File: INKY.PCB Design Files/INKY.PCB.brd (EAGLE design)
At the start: 55.8 x 40.9 mm, 34 parts, among them J1-PROG RJ45-8, J2 RJ45-8, U1 MC9S08SH8CTG, U3 RS485SOIC

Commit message: Still routing
~ 95% done
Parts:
- moved U3 2.00 mm to (-3.75, -6.22)
- moved U$14 1.31 mm to (8.45, 0.40)
- moved U$23 1.30 mm to (17.4, -9.20)
- moved U$21 1.21 mm to (16.6, -13.8)
- moved U$13 1.12 mm to (-0.90, -9.50)
- moved U$22 1.05 mm to (17.4, -11.6)
- moved U$20 0.65 mm to (0.00, -15.9)
- moved C1 0.47 mm to (-2.56, 11.7)
- moved U$2 0.40 mm to (-16.0, -17.6), flipped to the bottom
- moved U$8 0.40 mm to (-16.0, -17.6), flipped to the top
- moved U$5 0.35 mm to (10.4, -13.6)
- moved C2 0.34 mm to (2.04, 11.6)
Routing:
- net GND: track 123.3 -> 200.9 mm
- net +3V3: track 41.7 -> 105.7 mm
- net ACK: track 22.4 -> 70.4 mm, vias 0 -> 1
- net N$6: track 0.00 -> 39.7 mm, vias 0 -> 1
- net +5V: track 189.1 -> 221.6 mm, vias 2 -> 4
- net N$5: track 0.00 -> 30.3 mm, vias 0 -> 1
- net RST: track 3.00 -> 16.9 mm, vias 0 -> 1
- net RX: track 28.7 -> 14.8 mm
- net BDM: track 10.8 -> 5.22 mm, vias 0 -> 1
- net 485N: track 59.1 -> 61.5 mm
- net N$29: track 28.0 -> 30.2 mm
- net N$30: track 23.5 -> 25.4 mm
- net N$31: track 15.0 -> 16.7 mm
- net DIR: track 12.6 -> 11.0 mm
- net N$7: track 9.75 -> 8.25 mm
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
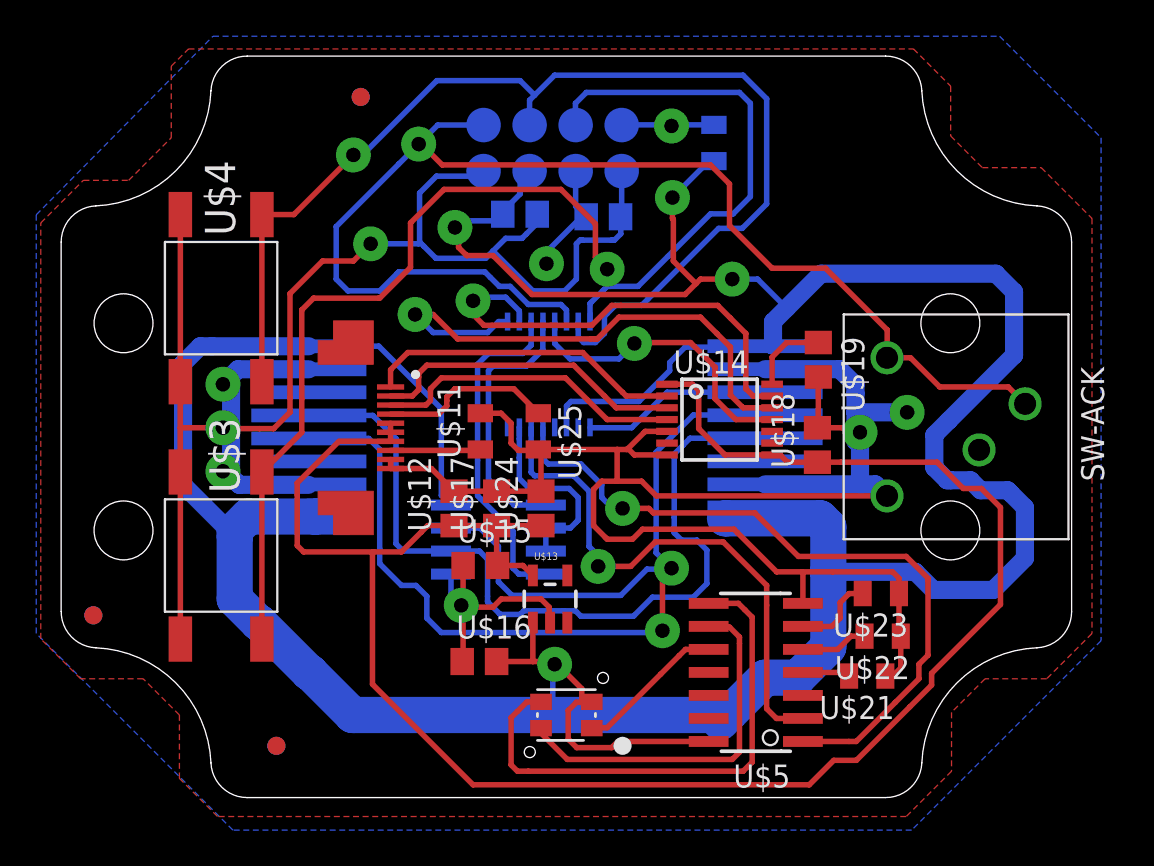
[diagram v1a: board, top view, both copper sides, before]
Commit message: Inky finishing
Done routing, need to fix angles.
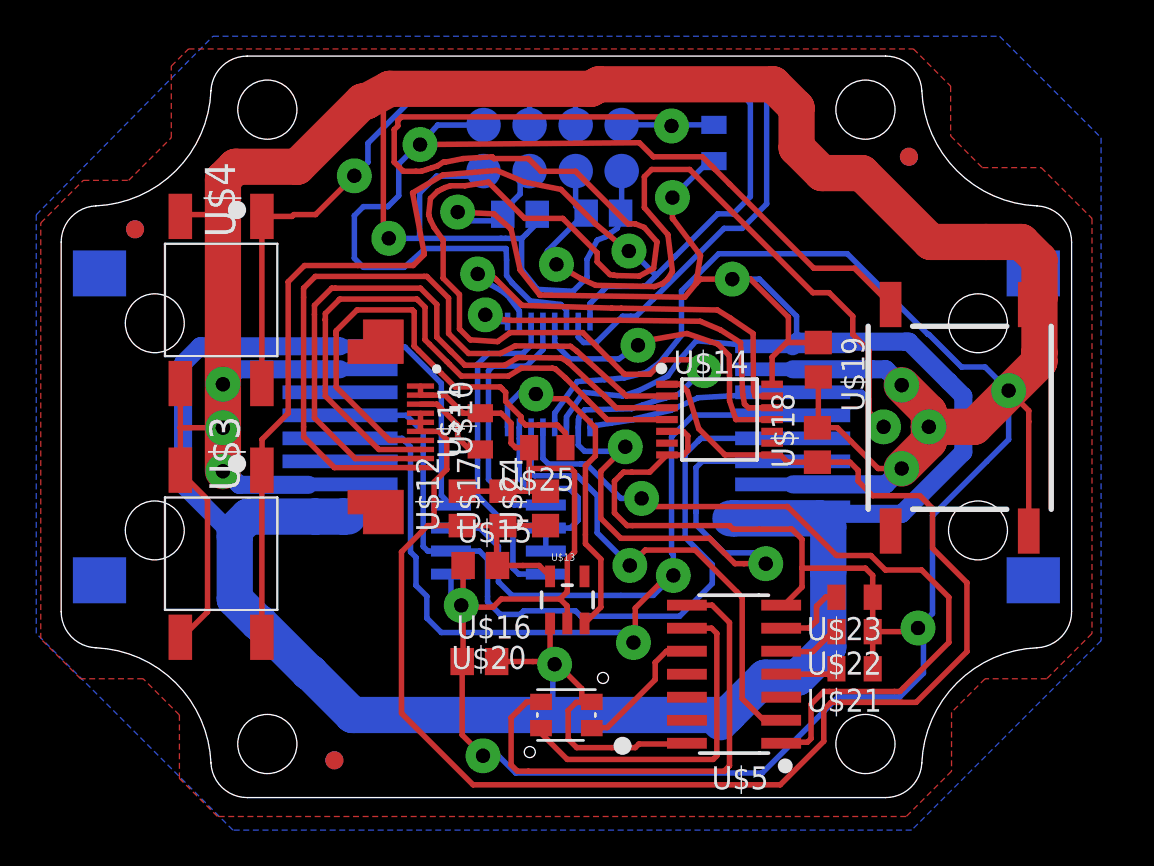
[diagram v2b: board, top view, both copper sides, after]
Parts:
- J1-PROG, J2: value RJ45-8 -> RJ45-8MOLEX_0955406886; device GW-devices:MOLEX-0955016649 -> GW-devices:RJ45_GUIDE
- SW-ACK: value SWITCH-TACTILE-320.01E11WHT -> SWITCH-TACTILE-5E/5GSH9; device GW-devices:SWITCH-TACTILE-320.01E11WHT -> GW-devices:SWITCH_TACTILE-5E/5GSH9
- U$10: value 52745-1097 -> (none); device KW2:52745-1097 -> KW2:FPC
- U$20: device KW2:RGBLED -> KW2:PLCC4_SMALL
- moved U$6 30.4 mm to (18.9, 14.9), flipped to the bottom
- moved U$9 30.4 mm to (18.9, 14.9), flipped to the top
- moved U$1 21.4 mm to (-23.8, 10.9)
- moved U$7 21.4 mm to (-23.8, 10.9)
- moved J2 11.9 mm to (-12.5, 0.00)
- moved J1-PROG 8.70 mm to (12.5, 0.00)
- moved U$2 3.30 mm to (-12.8, -18.4)
- moved U$8 3.30 mm to (-12.8, -18.4)
- moved U$10 1.65 mm to (-9.00, 0.00)
- moved U$22 1.57 mm to (15.9, -11.3)
- moved U$23 1.46 mm to (15.9, -9.40)
- moved U$5 1.20 mm to (9.25, -13.7)
- moved U$25 1.03 mm to (-1.05, -1.15), turned to 180 degrees
- moved U$13 0.95 mm to (0.05, -9.55)
- moved U$21 0.81 mm to (15.9, -13.3)
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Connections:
- removed net +3V3: U$10.P$5, U$10.P$6, U$10.P$7, U$12.1, U$13.5, U$14.1, U$14.8, U$15.2, U$17.1, U$18.1, U$24.1
- new net GMD: U$10.P$4, U$10.P$5, U$10.P$6, U$12.1, U$13.5, U$14.1, U$14.8, U$15.2, U$17.1, U$18.1, U$24.1
- net ACK: no longer SW-ACK.P$2
- net GND: now also U$10.P$1, U$10.P$2; no longer U$10.P$10, U$10.P$9
- net N$2: now also U$10.P$10; no longer U$10.P$1
- net N$3: now also U$10.P$9; no longer U$10.P$2
- net N$32: now also U$10.P$3; no longer U$10.P$8
- net N$33: now also U$10.P$7; no longer U$10.P$4
- net N$4: now also U$10.P$8; no longer U$10.P$3
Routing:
- net GND: track 200.9 -> 359.7 mm, vias 7 -> 11
- net BDM: track 5.22 -> 119.8 mm, vias 1 -> 4
- net +3V3: track 105.7 -> 0.00 mm
- net GMD: track 0.00 -> 94.8 mm
- net RST: track 16.9 -> 59.2 mm, vias 1 -> 2
- net N$2: track 17.6 -> 39.7 mm
- net N$3: track 17.5 -> 36.8 mm
- net N$1: track 0.00 -> 19.0 mm, vias 0 -> 1
- net N$33: track 9.58 -> 27.3 mm
- net N$4: track 17.2 -> 34.3 mm
- net ACK: track 70.4 -> 57.7 mm
- net +5V: track 221.6 -> 209.8 mm
- net N$29: track 30.2 -> 21.9 mm
- net INC_DOWN: track 72.9 -> 76.9 mm
- net N$5: track 30.3 -> 27.1 mm
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
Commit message: Inky v0.1
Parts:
- moved U1 0.20 mm to (-0.77, 2.89)
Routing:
- net GND: track 359.7 -> 358.6 mm
- net +5V: track 209.8 -> 208.9 mm
- net N$6: track 42.5 -> 41.7 mm
- net BDM: track 119.8 -> 120.5 mm
- net N$5: track 27.1 -> 26.4 mm
- net DIR: track 11.0 -> 10.4 mm
- net N$29: track 21.9 -> 21.3 mm

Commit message: Inky 0.2
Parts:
- U$11, U$25: value (none) -> 10K
- moved U$20 32.6 mm to (0.00, 16.7)
- moved U$5 31.2 mm to (-10.2, 10.7)
- moved U$21 28.2 mm to (-2.70, 7.85)
- moved U$22 28.1 mm to (-2.70, 9.70)
- moved U$23 28.0 mm to (-2.70, 11.5)
- moved U$16 17.3 mm to (12.4, -11.2), turned to 90 degrees
- moved U$15 17.2 mm to (12.4, -6.40), turned to 270 degrees
- moved U$12 15.5 mm to (7.85, -11.9), turned to 270 degrees
- moved U$17 15.4 mm to (10.0, -11.9), turned to 270 degrees
- moved U$13 15.1 mm to (15.1, -8.50)
- moved U$10 13.9 mm to (0.00, -10.6), turned to 0 degrees
- moved C2 13.1 mm to (15.1, 12.5), turned to 90 degrees
- moved U$24 11.5 mm to (9.85, -7.70)
- moved C1 7.38 mm to (-9.26, 8.63)
- moved U$11 6.55 mm to (-2.00, -6.20)
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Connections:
- net INC_DOWN: no longer U$3.2
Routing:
- net GND: track 358.6 -> 283.5 mm, vias 11 -> 12
- net BDM: track 120.5 -> 57.8 mm, vias 4 -> 3
- net GMD: track 94.8 -> 42.5 mm
- net +5V: track 208.9 -> 259.3 mm, vias 4 -> 5
- net N$1: track 18.9 -> 54.2 mm, vias 1 -> 3
- net ACK: track 57.9 -> 25.7 mm
- net N$6: track 41.7 -> 12.7 mm
- net N$33: track 27.3 -> 2.68 mm
- net N$2: track 39.9 -> 19.1 mm
- net INC_DOWN: track 76.5 -> 56.1 mm
- net N$3: track 37.0 -> 18.1 mm
- net N$4: track 34.4 -> 15.8 mm
- net RST: track 58.9 -> 42.6 mm, vias 2 -> 0
- net N$9: track 27.6 -> 12.6 mm
- net N$5: track 26.4 -> 11.6 mm
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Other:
- board text added: "INKY.PCB.v1.0P2"
- board text removed: "POSCON.PCB.v1.2"
